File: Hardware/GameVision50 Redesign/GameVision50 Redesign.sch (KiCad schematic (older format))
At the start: 29 parts, among them J1 Reset/Power, J2 Potentiometer, J3 USB_B_Mini, J4 Test Points, J5 Controller, J6 STLink, U1 AMS1117-3.3, U2 STM32F103C8Tx, U3 MCP130-xxxFxTO, Y1 8MHz

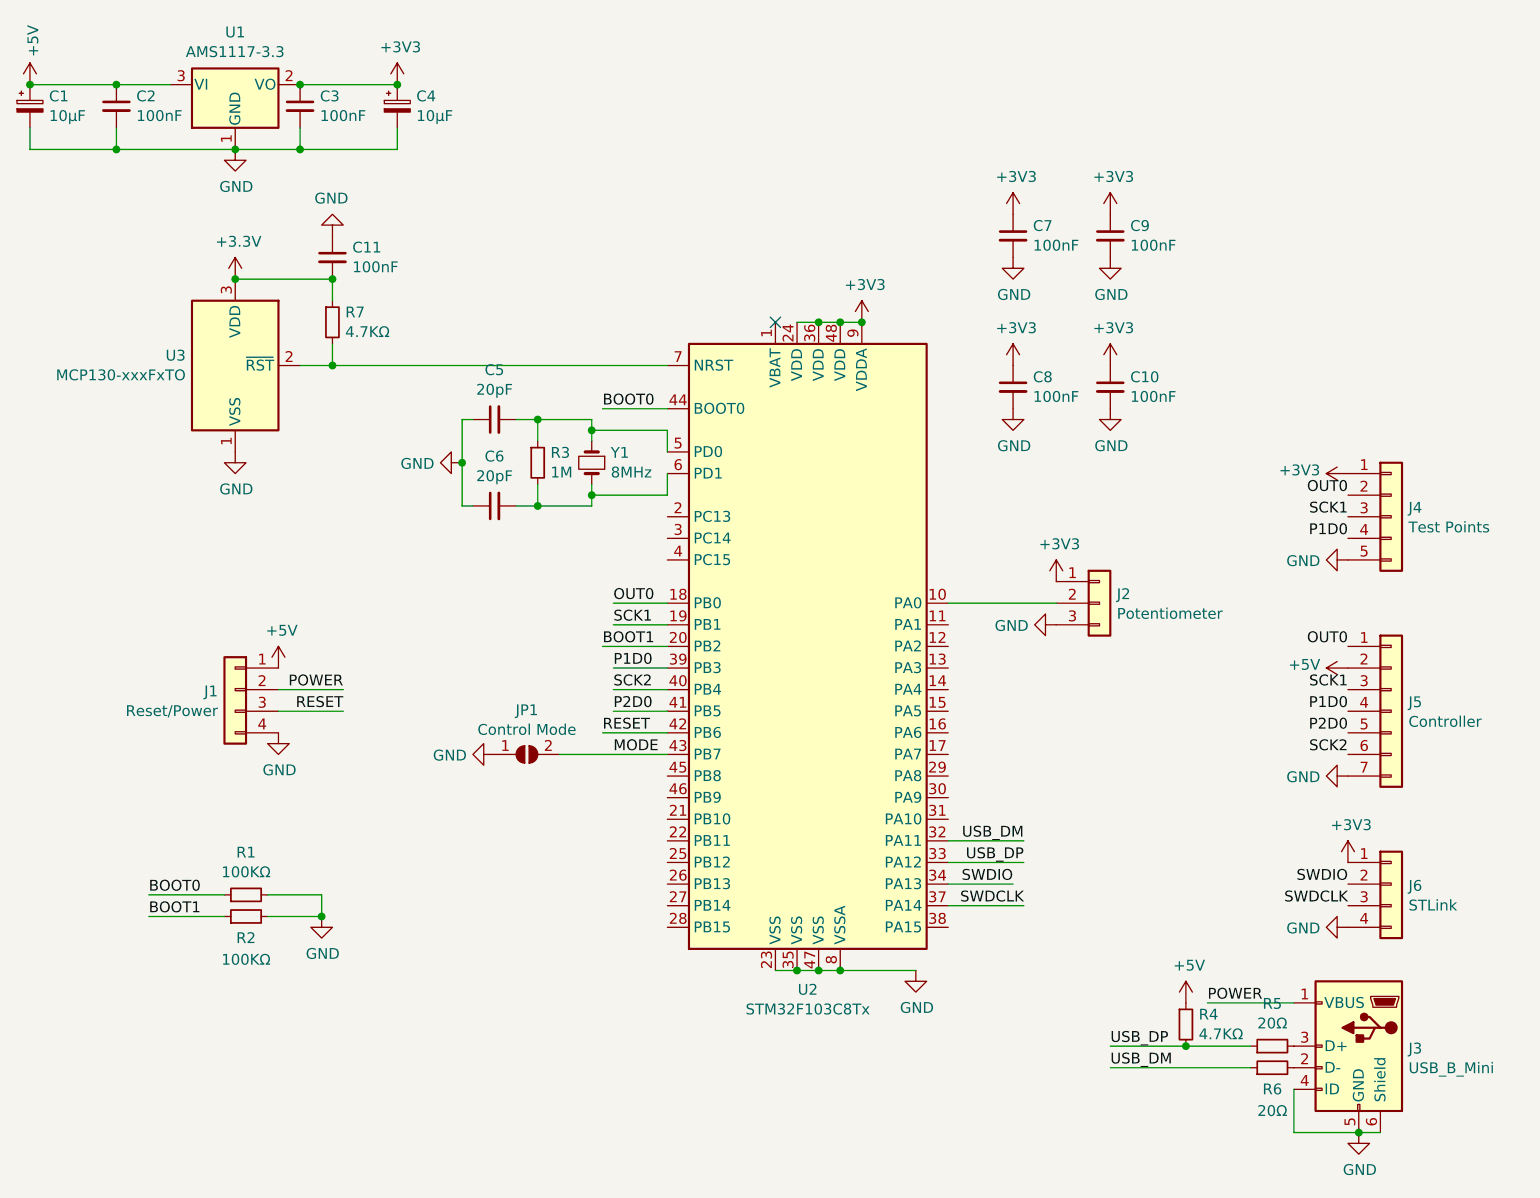
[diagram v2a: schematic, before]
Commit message: better footprint layout and 3d model of oscillator
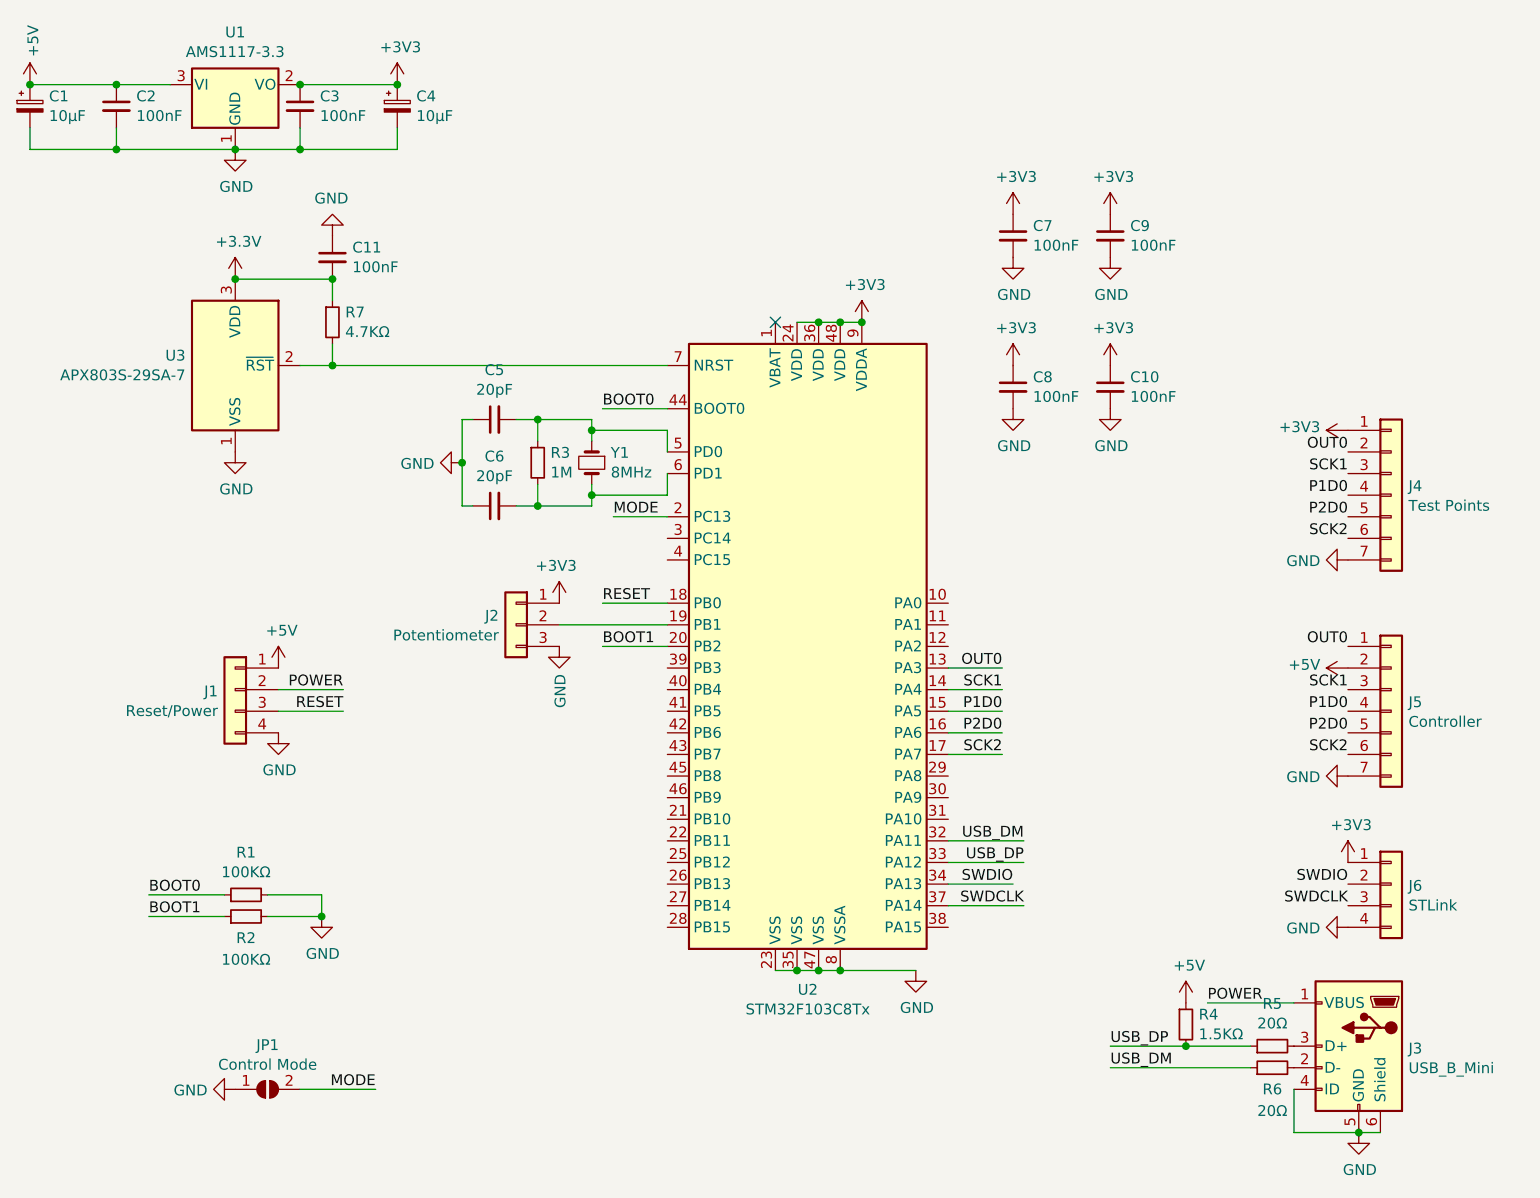
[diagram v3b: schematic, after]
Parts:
- removed J4: Test Points, Connector_PinHeader_2.54mm:PinHeader_1x05_P2.54mm_Vertical, symbol Connector_Generic:Conn_01x05
- added J4: Test Points, Connector_PinHeader_2.54mm:PinHeader_1x07_P2.54mm_Vertical, symbol Connector_Generic:Conn_01x07
- R4: value 4.7KΩ -> 1.5KΩ; LCSC C25900 -> C25867
- U3: value MCP130-xxxFxTO -> APX803S-29SA-7; footprint Package_TO_SOT_THT:TO-92_Inline -> Package_TO_SOT_SMD:SOT-23
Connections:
- net +3V3: now also J4.1 (Pin_1)
- net GND: now also J4.7 (Pin_7)
- net MODE: now also U2.2 (PC13); no longer U2.43 (PB7)
- net OUT0: now also U2.13 (PA3), J4.2 (Pin_2); no longer U2.18 (PB0)
- net P1D0: now also U2.15 (PA5), J4.4 (Pin_4); no longer U2.39 (PB3)
- net P2D0: now also U2.16 (PA6), J4.5 (Pin_5); no longer U2.41 (PB5)
- net RESET: now also U2.18 (PB0); no longer U2.42 (PB6)
- net SCK1: now also U2.14 (PA4), J4.3 (Pin_3); no longer U2.19 (PB1)
- net SCK2: now also U2.17 (PA7), J4.6 (Pin_6); no longer U2.40 (PB4)
- net at U2.10 (PA0): no longer J2.2 (Pin_2)
- new net: J2.2 (Pin_2), U2.19 (PB1)
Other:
- moved on the sheet: J2, JP1
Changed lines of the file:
@@
 L Connector_Generic:Conn_01x03 J2
 U 1 1 5ED97ED5
-P 6850 3300
-F 0 "J2" H 6930 3342 50  0000 L CNN
-F 1 "Potentiometer" H 6930 3251 50  0000 L CNN
-F 2 "Connector_PinHeader_2.54mm:PinHeader_1x03_P2.54mm_Vertical" H 6850 3300 50  0001 C CNN
-F 3 "~" H 6850 3300 50  0001 C CNN
-	1    6850 3300
-	1    0    0    -1
+P 4150 3400
+F 0 "J2" H 4230 3442 50  0000 L CNN
+F 1 "Potentiometer" H 4230 3351 50  0000 L CNN
+F 2 "Connector_PinHeader_2.54mm:PinHeader_1x03_P2.54mm_Vertical" H 4150 3400 50  0001 C CNN
+F 3 "~" H 4150 3400 50  0001 C CNN
+	1    4150 3400
+	-1   0    0    -1
 $EndComp
 $Comp
@@
 	0    1    1    0
 $EndComp
+Text Label 8000 2600 2    50   ~ 0
+OUT0
+Text Label 8000 2700 2    50   ~ 0
+SCK1
 Text Label 8000 2800 2    50   ~ 0
-OUT0
-Text Label 8000 2900 2    50   ~ 0
-SCK1
-Text Label 8000 3000 2    50   ~ 0
 P1D0
 $Comp
 L power:GND #PWR0102
 U 1 1 5EDA0451
-P 6650 3400
-F 0 "#PWR0102" H 6650 3150 50  0001 C CNN
-F 1 "GND" V 6655 3272 50  0000 R CNN
-F 2 "" H 6650 3400 50  0001 C CNN
-F 3 "" H 6650 3400 50  0001 C CNN
-	1    6650 3400
-	0    1    1    0
+P 4350 3500
+F 0 "#PWR0102" H 4350 3250 50  0001 C CNN
+F 1 "GND" V 4355 3372 50  0000 R CNN
+F 2 "" H 4350 3500 50  0001 C CNN
+F 3 "" H 4350 3500 50  0001 C CNN
+	1    4350 3500
+	1    0    0    -1
 $EndComp
 $Comp
 L power:+3V3 #PWR0103
 U 1 1 5EDA1680
-P 6650 3200
-F 0 "#PWR0103" H 6650 3050 50  0001 C CNN
-F 1 "+3V3" H 6665 3373 50  0000 C CNN
-F 2 "" H 6650 3200 50  0001 C CNN
-F 3 "" H 6650 3200 50  0001 C CNN
-	1    6650 3200
-	1    0    0    -1
+P 4350 3300
+F 0 "#PWR0103" H 4350 3150 50  0001 C CNN
+F 1 "+3V3" H 4365 3473 50  0000 C CNN
+F 2 "" H 4350 3300 50  0001 C CNN
+F 3 "" H 4350 3300 50  0001 C CNN
+	1    4350 3300
+	-1   0    0    -1
 $EndComp
 Text Label 6500 4500 2    50   ~ 0
@@
 Wire Wire Line
 	6500 4500 6150 4500
-Wire Wire Line
-	6150 3300 6650 3300
 Text Label 6450 4600 2    50   ~ 0
 SWDIO
@@
 POWER
 $Comp
-L Connector_Generic:Conn_01x05 J4
-U 1 1 5EDC5E59
-P 8200 2900
-F 0 "J4" H 8280 2942 50  0000 L CNN
-F 1 "Test Points" H 8280 2851 50  0000 L CNN
-F 2 "Connector_PinHeader_2.54mm:PinHeader_1x05_P2.54mm_Vertical" H 8200 2900 50  0001 C CNN
-F 3 "~" H 8200 2900 50  0001 C CNN
-	1    8200 2900
-	1    0    0    -1
-$EndComp
-$Comp
 L power:+3V3 #PWR0106
 U 1 1 5EDC70B1
-P 8000 2700
-F 0 "#PWR0106" H 8000 2550 50  0001 C CNN
-F 1 "+3V3" V 8015 2828 50  0000 L CNN
-F 2 "" H 8000 2700 50  0001 C CNN
-F 3 "" H 8000 2700 50  0001 C CNN
-	1    8000 2700
+P 8000 2500
+F 0 "#PWR0106" H 8000 2350 50  0001 C CNN
+F 1 "+3V3" V 8015 2628 50  0000 L CNN
+F 2 "" H 8000 2500 50  0001 C CNN
+F 3 "" H 8000 2500 50  0001 C CNN
+	1    8000 2500
 	0    -1   -1   0
 $EndComp
@@
 P 7250 5250
 F 0 "R4" H 7309 5296 50  0000 L CNN
-F 1 "4.7KΩ" H 7309 5205 50  0000 L CNN
+F 1 "1.5KΩ" H 7309 5205 50  0000 L CNN
 F 2 "Resistor_SMD:R_0402_1005Metric" H 7250 5250 50  0001 C CNN
 F 3 "~" H 7250 5250 50  0001 C CNN
-F 4 "C25900" H 7250 5250 50  0001 C CNN "LCSC"
+F 4 "C25867" H 7250 5250 50  0001 C CNN "LCSC"
 	1    7250 5250
 	1    0    0    -1
@@
 	0    -1   -1   0
 $EndComp
-Text Label 8000 4000 2    50   ~ 0
+Text Label 8000 3000 2    50   ~ 0
 SCK2
-Text Label 8000 3900 2    50   ~ 0
+Text Label 8000 2900 2    50   ~ 0
 P2D0
 Text Label 8000 3800 2    50   ~ 0
@@
 Wire Wire Line
 	5650 5000 6000 5000
-Text Label 4550 3900 0    50   ~ 0
+Text Label 4550 3300 0    50   ~ 0
 RESET
 Text Label 3350 3700 2    50   ~ 0
@@
 	1    0    0    -1
 $EndComp
-Text Label 4600 3300 0    50   ~ 0
+Text Label 6400 3600 2    50   ~ 0
 OUT0
-Text Label 4600 3400 0    50   ~ 0
-SCK1
-Text Label 4600 3600 0    50   ~ 0
+Text Label 6400 3800 2    50   ~ 0
 P1D0
 Wire Wire Line
 	4550 3500 4850 3500
-Wire Wire Line
-	4850 3600 4600 3600
-Wire Wire Line
-	4600 3400 4850 3400
-Wire Wire Line
-	4850 3300 4600 3300
 Text Label 3350 3800 2    50   ~ 0
 RESET
-Wire Wire Line
-	4550 3900 4850 3900
-Text Label 4600 3800 0    50   ~ 0
-P2D0
-Text Label 4600 3700 0    50   ~ 0
-SCK2
-Wire Wire Line
-	4600 3700 4850 3700
-Wire Wire Line
-	4600 3800 4850 3800
 Wire Wire Line
 	7350 5150 7750 5150
@@
 L Jumper:SolderJumper_2_Open JP1
 U 1 1 5EEBB07A
-P 4200 4000
-F 0 "JP1" H 4200 4205 50  0000 C CNN
-F 1 "Control Mode" H 4200 4114 50  0000 C CNN
-F 2 "Jumper:SolderJumper-2_P1.3mm_Open_TrianglePad1.0x1.5mm" H 4200 4000 50  0001 C CNN
-F 3 "~" H 4200 4000 50  0001 C CNN
-	1    4200 4000
+P 3000 5550
+F 0 "JP1" H 3000 5755 50  0000 C CNN
+F 1 "Control Mode" H 3000 5664 50  0000 C CNN
+F 2 "Jumper:SolderJumper-2_P1.3mm_Open_TrianglePad1.0x1.5mm" H 3000 5550 50  0001 C CNN
+F 3 "~" H 3000 5550 50  0001 C CNN
+	1    3000 5550
 	1    0    0    -1
 $EndComp
@@
 L power:GND #PWR0128
 U 1 1 5EEBFB5A
-P 4050 4000
-F 0 "#PWR0128" H 4050 3750 50  0001 C CNN
-F 1 "GND" V 4055 3872 50  0000 R CNN
-F 2 "" H 4050 4000 50  0001 C CNN
-F 3 "" H 4050 4000 50  0001 C CNN
-	1    4050 4000
+P 2850 5550
+F 0 "#PWR0128" H 2850 5300 50  0001 C CNN
+F 1 "GND" V 2855 5422 50  0000 R CNN
+F 2 "" H 2850 5550 50  0001 C CNN
+F 3 "" H 2850 5550 50  0001 C CNN
+	1    2850 5550
 	0    1    1    0
 $EndComp
-Wire Wire Line
-	4350 4000 4850 4000
-Text Label 4600 4000 0    50   ~ 0
-MODE
 $Comp
 L Device:C_Small C6
@@
 U 1 1 5EDAF659
 P 2850 2200
-F 0 "U3" H 2621 2246 50  0000 R CNN
-F 1 "MCP130-xxxFxTO" H 2621 2155 50  0000 R CNN
-F 2 "Package_TO_SOT_THT:TO-92_Inline" H 3500 1850 50  0001 C CNN
+F 0 "U3" H 2620 2246 50  0000 R CNN
+F 1 "APX803S-29SA-7" H 2620 2155 50  0000 R CNN
+F 2 "Package_TO_SOT_SMD:SOT-23" H 3500 1850 50  0001 C CNN
 F 3 "http://ww1.microchip.com/downloads/en/DeviceDoc/11184d.pdf" H 2850 2200 50  0001 C CNN
 F 4 "C143831" H 2850 2200 50  0001 C CNN "LCSC"
@@
 $EndComp
 Connection ~ 3300 1800
+Text Label 6400 3700 2    50   ~ 0
+SCK1
+Wire Wire Line
+	6150 3600 6400 3600
+Wire Wire Line
+	6150 3700 6400 3700
+Wire Wire Line
+	6150 3800 6400 3800
+Wire Wire Line
+	6150 3900 6400 3900
+Text Label 6400 4000 2    50   ~ 0
+SCK2
+Text Label 6400 3900 2    50   ~ 0
+P2D0
+Wire Wire Line
+	6400 4000 6150 4000
+$Comp
+L Connector_Generic:Conn_01x07 J4
+U 1 1 5EDC6B0E
+P 8200 2800
+F 0 "J4" H 8280 2842 50  0000 L CNN
+F 1 "Test Points" H 8280 2751 50  0000 L CNN
+F 2 "Connector_PinHeader_2.54mm:PinHeader_1x07_P2.54mm_Vertical" H 8200 2800 50  0001 C CNN
+F 3 "~" H 8200 2800 50  0001 C CNN
+	1    8200 2800
+	1    0    0    -1
+$EndComp
+Text Label 8000 3900 2    50   ~ 0
+P2D0
+Text Label 8000 4000 2    50   ~ 0
+SCK2
+Wire Wire Line
+	4350 3400 4850 3400
+Text Label 3500 5550 2    50   ~ 0
+MODE
+Text Label 4600 2900 0    50   ~ 0
+MODE
+Wire Wire Line
+	4600 2900 4850 2900
+Wire Wire Line
+	3150 5550 3500 5550
+Wire Wire Line
+	4550 3300 4850 3300
 $EndSCHEMATC

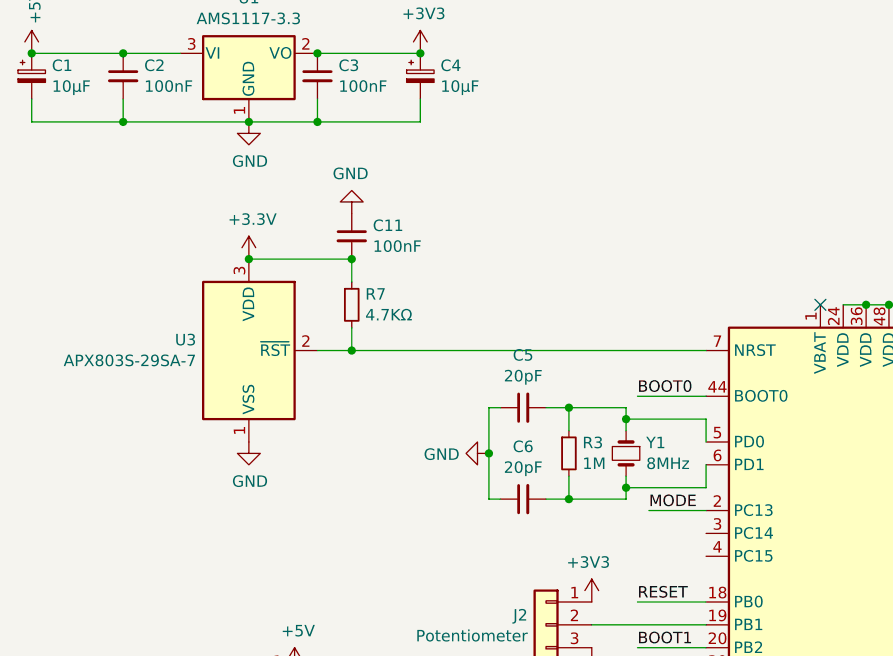
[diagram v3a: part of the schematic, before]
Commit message: exported version 1 of PCB to manufacture
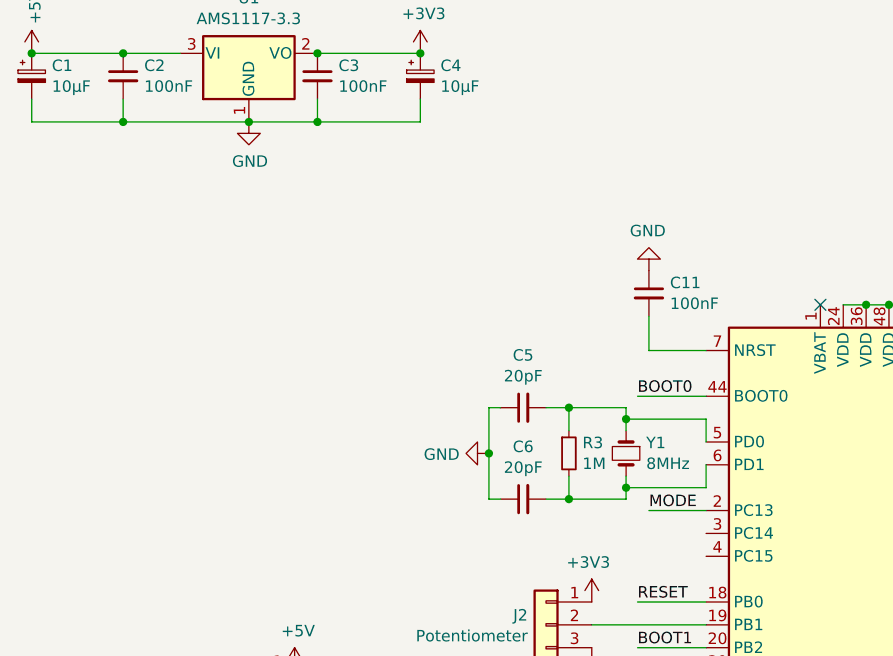
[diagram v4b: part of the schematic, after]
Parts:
- removed R7: 4.7KΩ, Resistor_SMD:R_0402_1005Metric, symbol Device:R_Small
- removed U3: APX803S-29SA-7, Package_TO_SOT_SMD:SOT-23, symbol Power_Supervisor:MCP130-xxxFxTO
- U1: LCSC (none) -> C6186
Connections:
- net +3V3: no longer C11.2
- net at U2.7 (NRST): now also C11.2
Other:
- moved on the sheet: C11
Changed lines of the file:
@@
 	4550 2400 4850 2400
-$Comp
-L Power_Supervisor:MCP130-xxxFxTO U3
-U 1 1 5EDAF659
-P 2850 2200
-F 0 "U3" H 2620 2246 50  0000 R CNN
-F 1 "APX803S-29SA-7" H 2620 2155 50  0000 R CNN
-F 2 "Package_TO_SOT_SMD:SOT-23" H 3500 1850 50  0001 C CNN
-F 3 "http://ww1.microchip.com/downloads/en/DeviceDoc/11184d.pdf" H 2850 2200 50  0001 C CNN
-F 4 "C143831" H 2850 2200 50  0001 C CNN "LCSC"
-	1    2850 2200
-	1    0    0    -1
-$EndComp
-$Comp
-L power:GND #PWR02
-U 1 1 5EDB0AB2
-P 2850 2600
-F 0 "#PWR02" H 2850 2350 50  0001 C CNN
-F 1 "GND" H 2855 2427 50  0000 C CNN
-F 2 "" H 2850 2600 50  0001 C CNN
-F 3 "" H 2850 2600 50  0001 C CNN
-	1    2850 2600
-	1    0    0    -1
-$EndComp
-$Comp
-L power:+3.3V #PWR01
-U 1 1 5EDB0F7B
-P 2850 1800
-F 0 "#PWR01" H 2850 1650 50  0001 C CNN
-F 1 "+3.3V" H 2865 1973 50  0000 C CNN
-F 2 "" H 2850 1800 50  0001 C CNN
-F 3 "" H 2850 1800 50  0001 C CNN
-	1    2850 1800
-	1    0    0    -1
-$EndComp
-$Comp
-L Device:R_Small R7
-U 1 1 5EDB3C95
-P 3300 2000
-F 0 "R7" H 3359 2046 50  0000 L CNN
-F 1 "4.7KΩ" H 3359 1955 50  0000 L CNN
-F 2 "Resistor_SMD:R_0402_1005Metric" H 3300 2000 50  0001 C CNN
-F 3 "~" H 3300 2000 50  0001 C CNN
-F 4 "C25900" H 3300 2000 50  0001 C CNN "LCSC"
-	1    3300 2000
-	1    0    0    -1
-$EndComp
-Wire Wire Line
-	2850 1800 3300 1800
-Wire Wire Line
-	3300 1800 3300 1900
-Connection ~ 2850 1800
-Wire Wire Line
-	3150 2200 3300 2200
-Wire Wire Line
-	3300 2200 3300 2100
-Wire Wire Line
-	4850 2200 3300 2200
-Connection ~ 3300 2200
 $Comp
 L power:+5V #PWR0104
@@
 F 2 "Package_TO_SOT_SMD:SOT-223-3_TabPin2" H 2850 1100 50  0001 C CNN
 F 3 "http://www.advanced-monolithic.com/pdf/ds1117.pdf" H 2950 650 50  0001 C CNN
+F 4 "C6186" H 2850 900 50  0001 C CNN "LCSC"
 	1    2850 900
 	1    0    0    -1
@@
 L power:GND #PWR03
 U 1 1 5EDE0288
-P 3300 1600
-F 0 "#PWR03" H 3300 1350 50  0001 C CNN
-F 1 "GND" H 3305 1427 50  0000 C CNN
-F 2 "" H 3300 1600 50  0001 C CNN
-F 3 "" H 3300 1600 50  0001 C CNN
-	1    3300 1600
+P 4600 1850
+F 0 "#PWR03" H 4600 1600 50  0001 C CNN
+F 1 "GND" H 4605 1677 50  0000 C CNN
+F 2 "" H 4600 1850 50  0001 C CNN
+F 3 "" H 4600 1850 50  0001 C CNN
+	1    4600 1850
 	-1   0    0    1
 $EndComp
@@
 L Device:C_Small C11
 U 1 1 5EDE028F
-P 3300 1700
-F 0 "C11" H 3392 1746 50  0000 L CNN
-F 1 "100nF" H 3392 1655 50  0000 L CNN
-F 2 "Capacitor_SMD:C_0402_1005Metric" H 3300 1700 50  0001 C CNN
-F 3 "~" H 3300 1700 50  0001 C CNN
-F 4 "C1525" H 3300 1700 50  0001 C CNN "LCSC"
-	1    3300 1700
+P 4600 1950
+F 0 "C11" H 4692 1996 50  0000 L CNN
+F 1 "100nF" H 4692 1905 50  0000 L CNN
+F 2 "Capacitor_SMD:C_0402_1005Metric" H 4600 1950 50  0001 C CNN
+F 3 "~" H 4600 1950 50  0001 C CNN
+F 4 "C1525" H 4600 1950 50  0001 C CNN "LCSC"
+	1    4600 1950
 	1    0    0    -1
 $EndComp
-Connection ~ 3300 1800
 Text Label 6400 3700 2    50   ~ 0
 SCK1
@@
 Wire Wire Line
 	4550 3300 4850 3300
+Wire Wire Line
+	4850 2200 4600 2200
+Wire Wire Line
+	4600 2200 4600 2050
 $EndSCHEMATC
